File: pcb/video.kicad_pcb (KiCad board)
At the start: 4 copper layers, 159.9 x 99.9 mm, 174 parts, among them J1 09031966921, J3 Conn_01x06, J4 Conn_01x06, J5 Conn_01x06, J6 Conn_01x06, J7 DB15_Female_HighDensity, J8 HDMI_A, U1 NCP115, U10 NCA9306DPH, U2 LP3853ESX-3.3/NOPB, U3 LCMXO2-1200HC-4TG100I, U4 LCMXO2-7000HC-4TG144C, U5 THS8136, U6 TFP410PAP, U7 ESD224DQA, U8 ESD224DQA, U9 PCA9540BDP, X1 ASV-xxxMHz

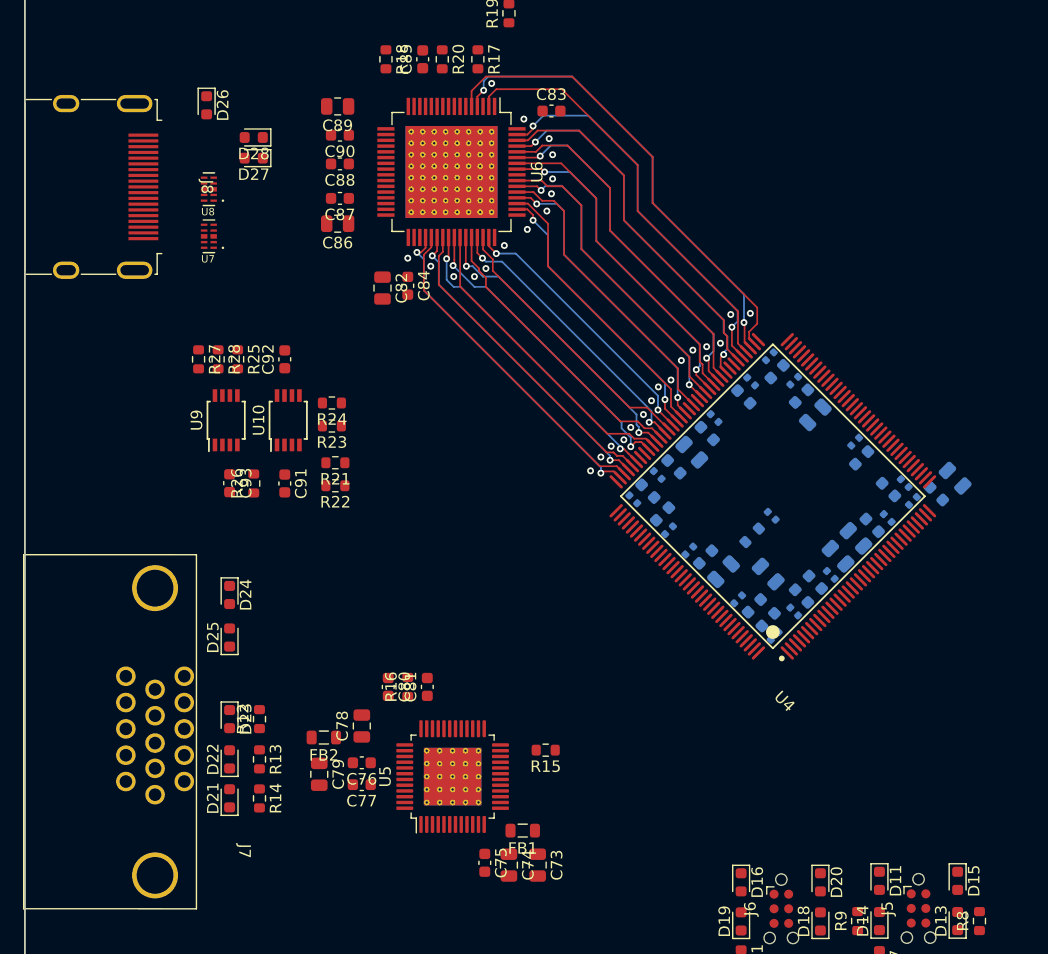
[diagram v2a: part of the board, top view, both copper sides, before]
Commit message: change the bank for the hdmi interface
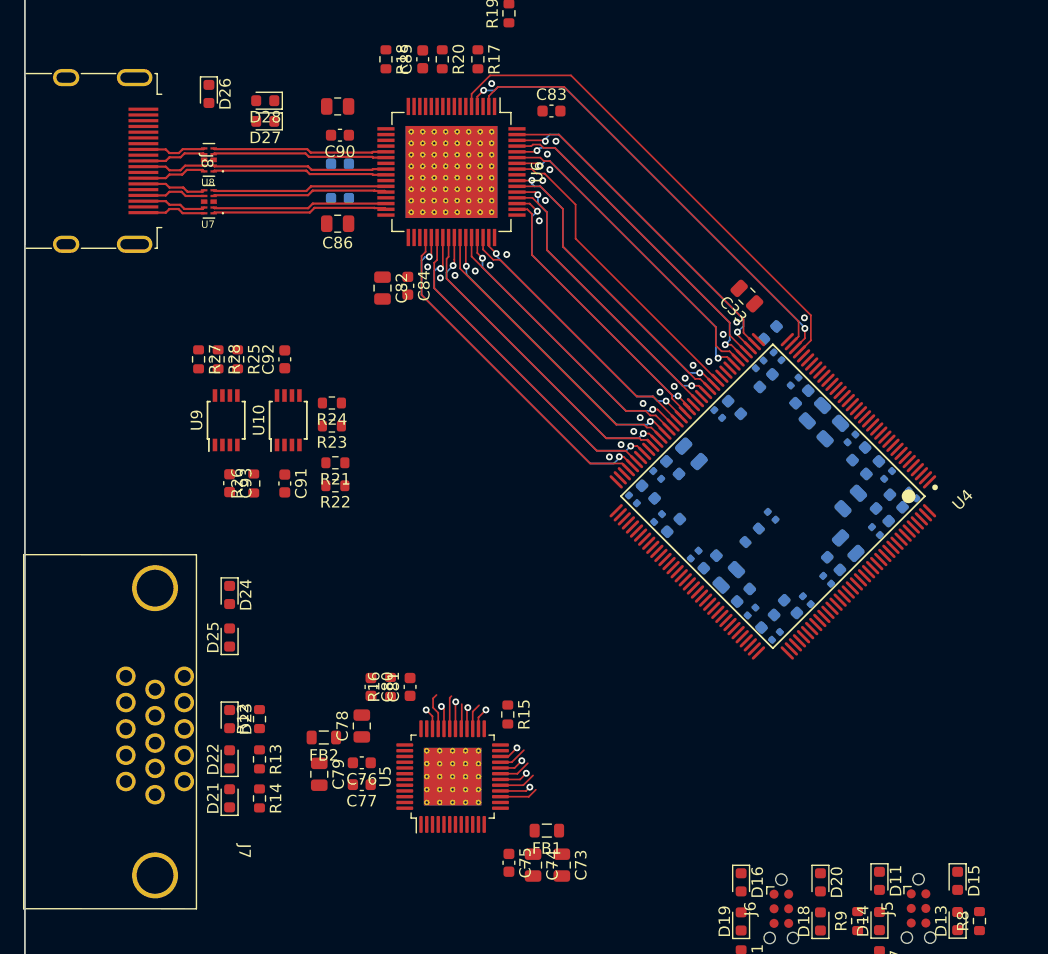
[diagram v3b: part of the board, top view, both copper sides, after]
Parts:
- C33: moved to F.Cu
- C87, C88: moved to B.Cu
- moved C33 24.1 mm to (117.9, 78.6), turned to 135 degrees
- moved C37 20.1 mm to (119.9, 81.8), turned to 45 degrees
- moved C41 17.2 mm to (120.5, 83.9), turned to -45 degrees
- moved C40 17.2 mm to (108.0, 96.3), turned to -45 degrees
- moved C39 17.2 mm to (120.4, 108.2), turned to 45 degrees
- moved C38 17.2 mm to (132.3, 95.9), turned to 135 degrees
- moved C62 16.3 mm to (119.0, 84.6), turned to -135 degrees
- moved C35 15.4 mm to (119.7, 106.9), turned to 45 degrees
- moved C34 15.3 mm to (109.3, 95.7), turned to -45 degrees
- moved C36 15.2 mm to (130.9, 96.5), turned to 135 degrees
- moved C63 14.5 mm to (110.1, 94.2), turned to -45 degrees
- moved C71 14.4 mm to (130.2, 94.2), turned to -135 degrees
- moved C49 14.4 mm to (118.3, 106.1), turned to 45 degrees
- moved C51 14.4 mm to (110.2, 97.9), turned to 45 degrees
- moved C58 14.4 mm to (122.0, 86.1), turned to -135 degrees
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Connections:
- net /HDMI frontend/D0_M renamed /HDMI frontend/D0_N
- net /HDMI frontend/D1_M renamed /HDMI frontend/D1_N
- net /HDMI frontend/D2_M renamed /HDMI frontend/D2_N
- net /HDMI frontend/DC_M renamed /HDMI frontend/DC_N
- net /HDMI frontend/TX0_M renamed /HDMI frontend/TX0_N
- net /HDMI frontend/TX1_M renamed /HDMI frontend/TX1_N
- net /HDMI frontend/TX2_M renamed /HDMI frontend/TX2_N
- net /HDMI frontend/TXC_M renamed /HDMI frontend/TXC_N
- U4 pad 100: HDMI_D18 -> VGA_B6
- U4 pad 103: HDMI_D19 -> VGA_B7
- U4 pad 104: HDMI_D20 -> unconnected-(U4B-PR3B/R_GPLLC_IN/(DQ0))
- U4 pad 105: HDMI_D21 -> unconnected-(U4B-PR3A/R_GPLLT_IN/(DQ0))
- U4 pad 106: HDMI_D22 -> unconnected-(U4B-PR2B/R_GPLLC_FB/(DQ0))
- U4 pad 107: HDMI_D23 -> unconnected-(U4B-PR2A/R_GPLLT_FB/(DQ0))
- U4 pad 33: unconnected-(U4D-PL24B) -> HDMI_VSYNC
- U4 pad 34: unconnected-(U4D-PL25A) -> HDMI_HSYNC
- U4 pad 35: unconnected-(U4D-PL25B) -> HDMI_DE
- U4 pad 38: unconnected-(U4C-PB4A) -> HDMI_D0
- U4 pad 39: unconnected-(U4C-PB4B) -> HDMI_D1
- U4 pad 40: unconnected-(U4C-PB6A/CSSPIN) -> HDMI_D2
- U4 pad 41: unconnected-(U4C-PB6B) -> HDMI_D3
- U4 pad 42: unconnected-(U4C-PB9A) -> HDMI_D4
- U4 pad 43: unconnected-(U4C-PB9B) -> HDMI_D5
- U4 pad 47: unconnected-(U4C-PB13A) -> HDMI_CLK
- U4 pad 48: unconnected-(U4C-PB13B) -> HDMI_D6
- U4 pad 49: unconnected-(U4C-PB16A/PCLKT2_0) -> HDMI_D7
- U4 pad 50: unconnected-(U4C-PB16B/PCLKC2_0) -> HDMI_D8
- U4 pad 52: unconnected-(U4C-PB18A) -> HDMI_D9
- U4 pad 54: unconnected-(U4C-PB18B) -> HDMI_D10
- U4 pad 55: unconnected-(U4C-PB23A/PCLKT2_1) -> HDMI_D11
- U4 pad 56: unconnected-(U4C-PB23B/PCLKC2_1) -> HDMI_D12
- U4 pad 57: unconnected-(U4C-PB26A) -> HDMI_D13
- U4 pad 58: unconnected-(U4C-PB26B) -> HDMI_D14
- U4 pad 59: unconnected-(U4C-PB29A) -> HDMI_D15
- U4 pad 60: unconnected-(U4C-PB29B) -> HDMI_D16
- U4 pad 61: unconnected-(U4C-PB31A) -> HDMI_D17
- U4 pad 62: unconnected-(U4C-PB31B) -> HDMI_D18
- U4 pad 63: unconnected-(U4C-PB31D) -> HDMI_D19
- U4 pad 65: unconnected-(U4C-PB35A) -> HDMI_D20
- U4 pad 67: unconnected-(U4C-PB35B) -> HDMI_D21
- U4 pad 68: unconnected-(U4C-PB37A) -> HDMI_D22
- U4 pad 69: unconnected-(U4C-PB37B) -> HDMI_D23
- U4 pad 70: unconnected-(U4C-PB38A/SN) -> /Video FPGA/SN
- U4 pad 73: unconnected-(U4B-PR24B/(DQ1)) -> VGA_G0
- U4 pad 74: HDMI_VSYNC -> VGA_G1
- U4 pad 75: HDMI_HSYNC -> VGA_G2
- U4 pad 76: HDMI_DE -> VGA_G3
- U4 pad 77: HDMI_D0 -> VGA_G4
- U4 pad 78: HDMI_D1 -> VGA_G5
- U4 pad 81: HDMI_D2 -> VGA_G6
- U4 pad 82: HDMI_D3 -> VGA_G7
- U4 pad 83: HDMI_D4 -> VGA_CLK
- U4 pad 84: HDMI_D5 -> VGA_R7
- U4 pad 85: HDMI_CLK -> VGA_R6
- U4 pad 86: HDMI_D6 -> VGA_R5
- U4 pad 87: HDMI_D7 -> VGA_R4
- U4 pad 89: HDMI_D8 -> VGA_R3
- U4 pad 91: HDMI_D9 -> VGA_R2
- U4 pad 92: HDMI_D10 -> VGA_R1
- U4 pad 93: HDMI_D11 -> VGA_R0
- U4 pad 94: HDMI_D12 -> VGA_B0
- U4 pad 95: HDMI_D13 -> VGA_B1
- U4 pad 96: HDMI_D14 -> VGA_B2
- U4 pad 97: HDMI_D15 -> VGA_B3
- U4 pad 98: HDMI_D16 -> VGA_B4
- U4 pad 99: HDMI_D17 -> VGA_B5
- U5 pad 1: VGA_B9 -> VGA_B7
- U5 pad 10: VGA_B0 -> GND
- U5 pad 13: VGA_R0 -> GND
- U5 pad 14: VGA_R1 -> GND
- U5 pad 15: VGA_R2 -> VGA_R0
- U5 pad 16: VGA_R3 -> VGA_R1
- U5 pad 17: VGA_R4 -> VGA_R2
- U5 pad 18: VGA_R5 -> VGA_R3
- U5 pad 19: VGA_R6 -> VGA_R4
- U5 pad 2: VGA_B8 -> VGA_B6
- U5 pad 20: VGA_R7 -> VGA_R5
- U5 pad 21: VGA_R8 -> VGA_R6
- U5 pad 22: VGA_R9 -> VGA_R7
- U5 pad 27: VGA_G9 -> VGA_G7
- U5 pad 28: VGA_G8 -> VGA_G6
- U5 pad 29: VGA_G7 -> VGA_G5
- U5 pad 3: VGA_B7 -> VGA_B5
- U5 pad 30: VGA_G6 -> VGA_G4
- U5 pad 31: VGA_G5 -> VGA_G3
- U5 pad 32: VGA_G4 -> VGA_G2
- U5 pad 33: VGA_G3 -> VGA_G1
- U5 pad 34: VGA_G2 -> VGA_G0
- U5 pad 35: VGA_G1 -> unconnected-(U5-G1)
- U5 pad 36: VGA_G0 -> GND
- U5 pad 4: VGA_B6 -> VGA_B4
- U5 pad 49: (no net) -> GND
- U5 pad 5: VGA_B5 -> VGA_B3
- U5 pad 6: VGA_B4 -> VGA_B2
- U5 pad 7: VGA_B3 -> VGA_B1
- U5 pad 8: VGA_B2 -> VGA_B0
- U5 pad 9: VGA_B1 -> GND
- U6 pad 65: unconnected-(U6B-EP) -> GND
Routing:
- net /HDMI frontend/TX2_P: track 0.00 -> 15.2 mm
- net /HDMI frontend/TX1_P: track 0.00 -> 15.2 mm
- net /HDMI frontend/TX2_N: track 0.00 -> 15.2 mm
- net /HDMI frontend/TX1_N: track 0.00 -> 15.2 mm
- net /HDMI frontend/TXC_P: track 0.00 -> 15.2 mm
- net /HDMI frontend/TX0_P: track 0.00 -> 15.2 mm
- net /HDMI frontend/TX0_N: track 0.00 -> 15.2 mm
- net /HDMI frontend/TXC_N: track 0.00 -> 15.2 mm
- net /HDMI frontend/D0_P: track 0.00 -> 5.63 mm
- net /HDMI frontend/D1_N: track 0.00 -> 5.62 mm
- net /HDMI frontend/D2_N: track 0.00 -> 5.62 mm
- net /HDMI frontend/DC_P: track 0.00 -> 5.58 mm
- net /HDMI frontend/DC_N: track 0.00 -> 5.58 mm
- net /HDMI frontend/D0_N: track 0.00 -> 5.58 mm
- net /HDMI frontend/D1_P: track 0.00 -> 5.56 mm
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
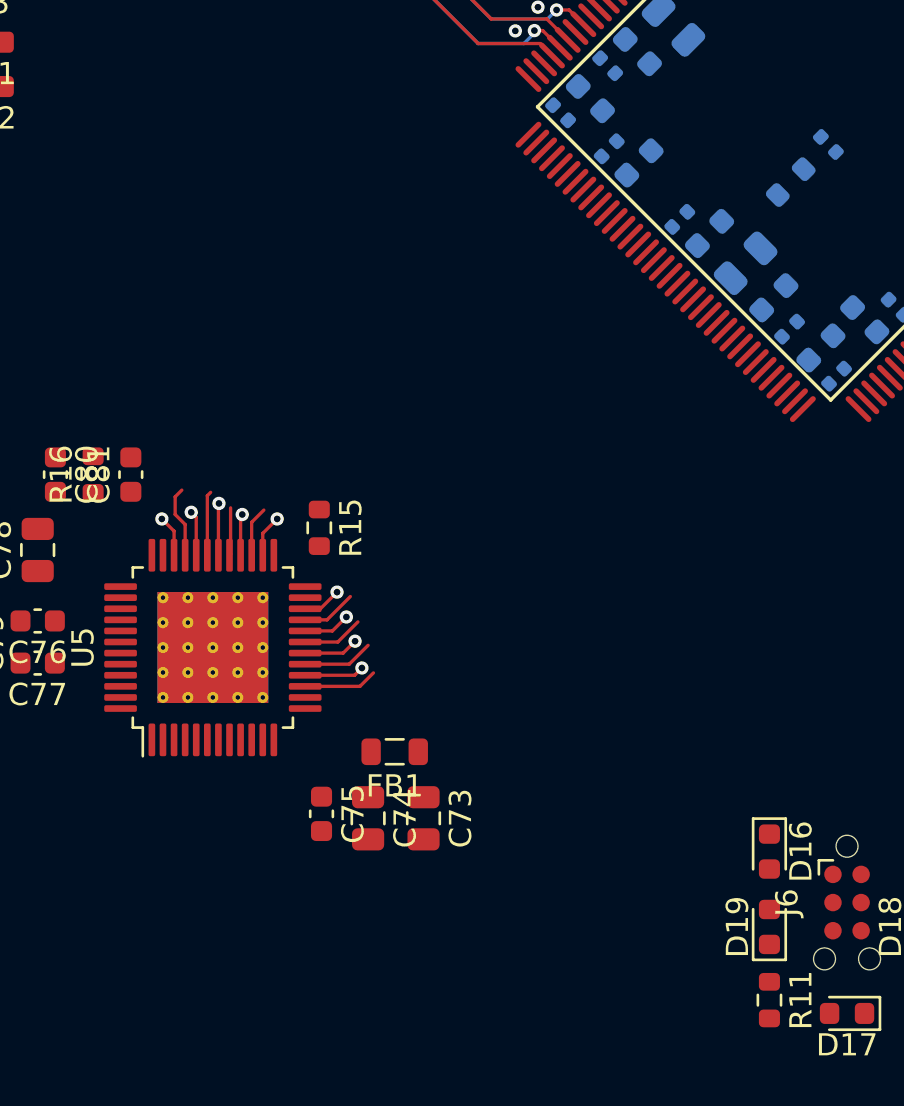
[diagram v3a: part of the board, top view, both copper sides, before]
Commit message: add traces to the vga interface minimizing crosstalk
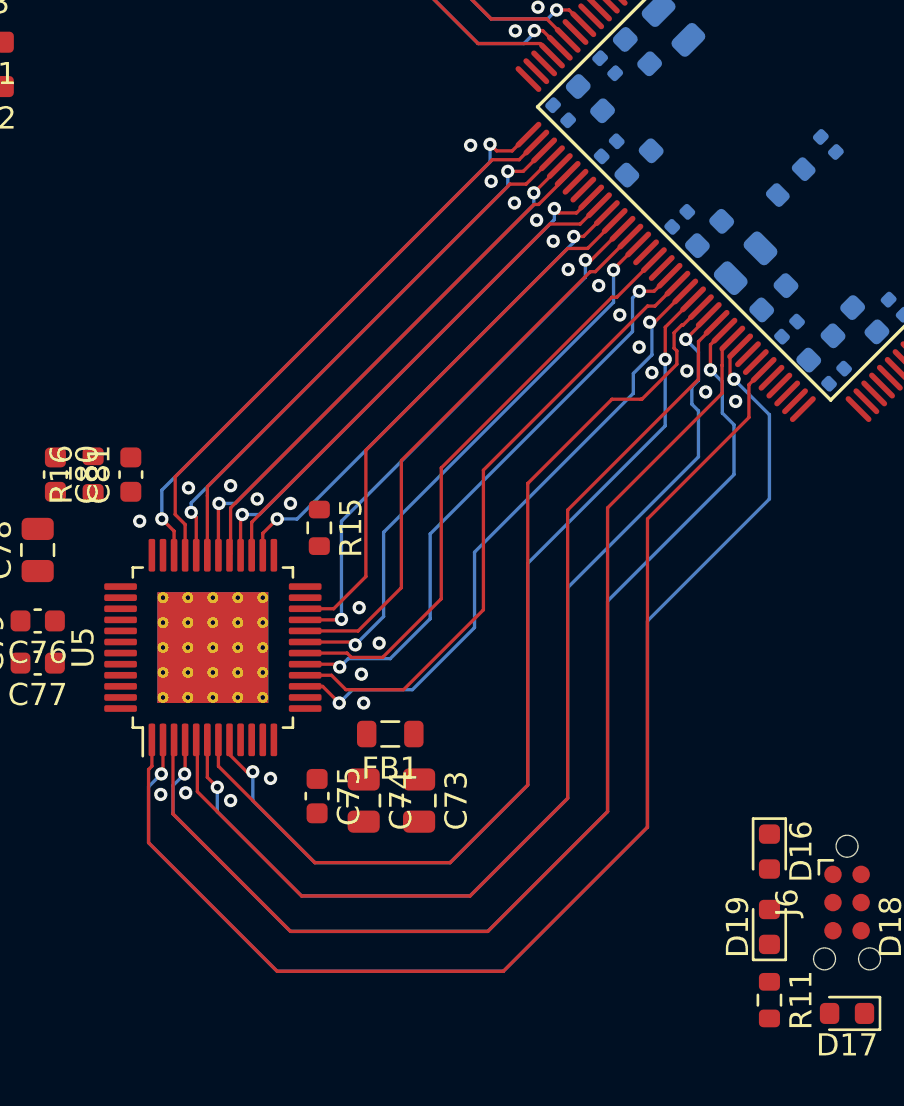
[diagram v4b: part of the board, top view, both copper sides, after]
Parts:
- moved C75 0.82 mm to (97.0, 127.1)
- moved C73 0.82 mm to (101.6, 127.3)
- moved C74 0.82 mm to (99.1, 127.3)
- moved FB1 0.82 mm to (100.3, 124.3)
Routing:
- net VGA_B6: track 0.00 -> 57.4 mm, vias 0 -> 2
- net VGA_B7: track 0.00 -> 55.1 mm
- net VGA_B4: track 0.00 -> 52.3 mm, vias 0 -> 2
- net VGA_B5: track 0.00 -> 51.1 mm
- net VGA_B2: track 0.00 -> 47.8 mm, vias 0 -> 2
- net VGA_B3: track 0.00 -> 47.1 mm
- net VGA_B1: track 0.00 -> 44.1 mm
- net VGA_B0: track 0.00 -> 43.3 mm, vias 0 -> 2
- net VGA_R1: track 2.69 -> 28.3 mm, vias 1 -> 0
- net VGA_R0: track 3.33 -> 28.7 mm, vias 0 -> 2
- net VGA_G0: track 1.87 -> 27.1 mm, vias 1 -> 2
- net VGA_R3: track 2.47 -> 26.7 mm, vias 1 -> 0
- net VGA_R2: track 3.19 -> 26.9 mm, vias 0 -> 2
- net VGA_G2: track 2.03 -> 25.4 mm, vias 1 -> 2
- net VGA_R5: track 2.12 -> 25.4 mm, vias 1 -> 0
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
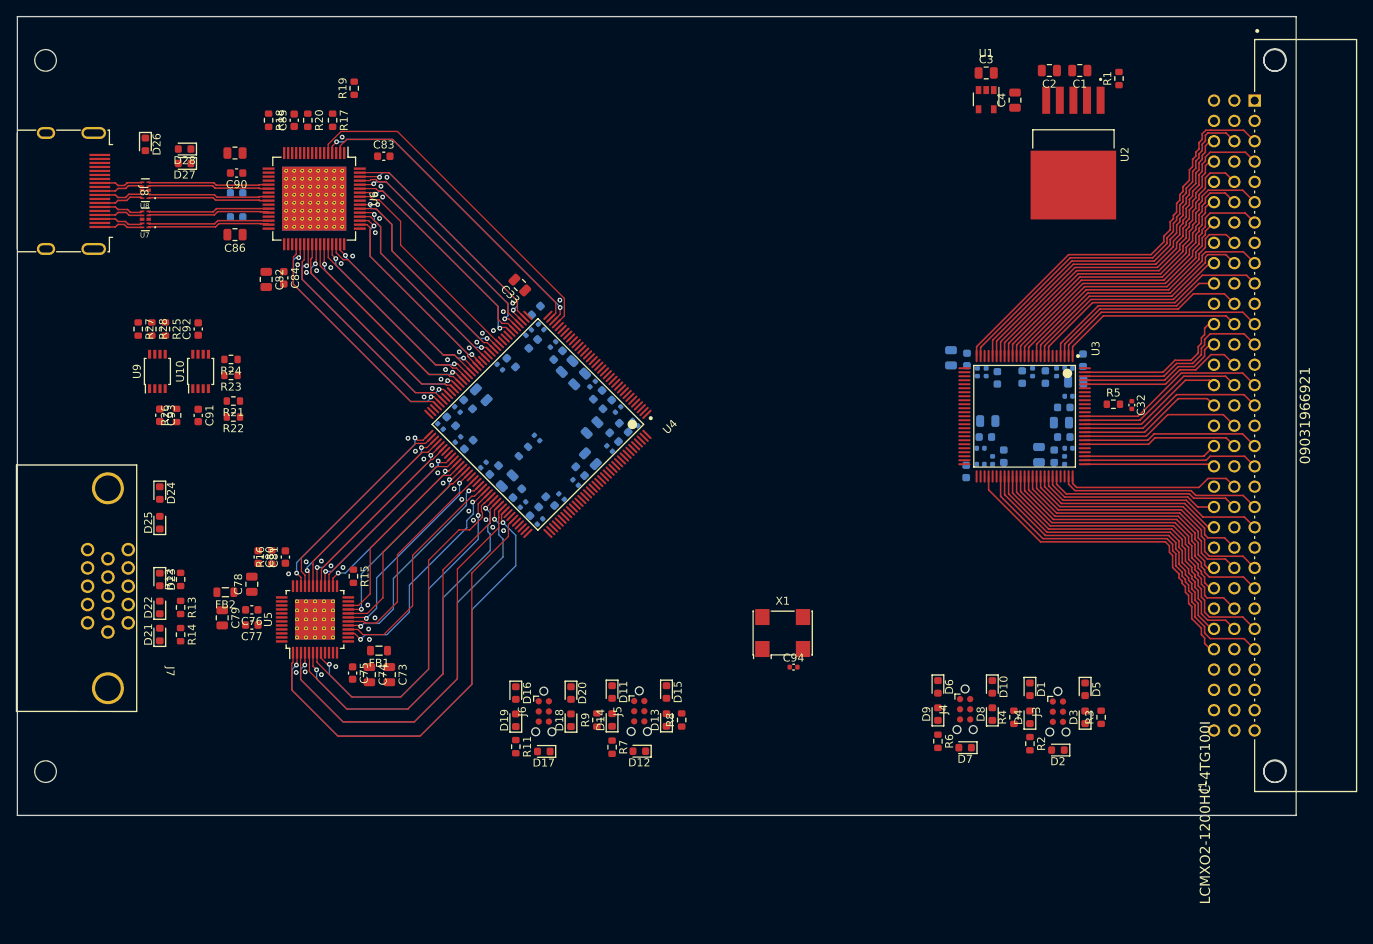
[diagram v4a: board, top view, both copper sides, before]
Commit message: add traces for the bus with crosstalk reduction
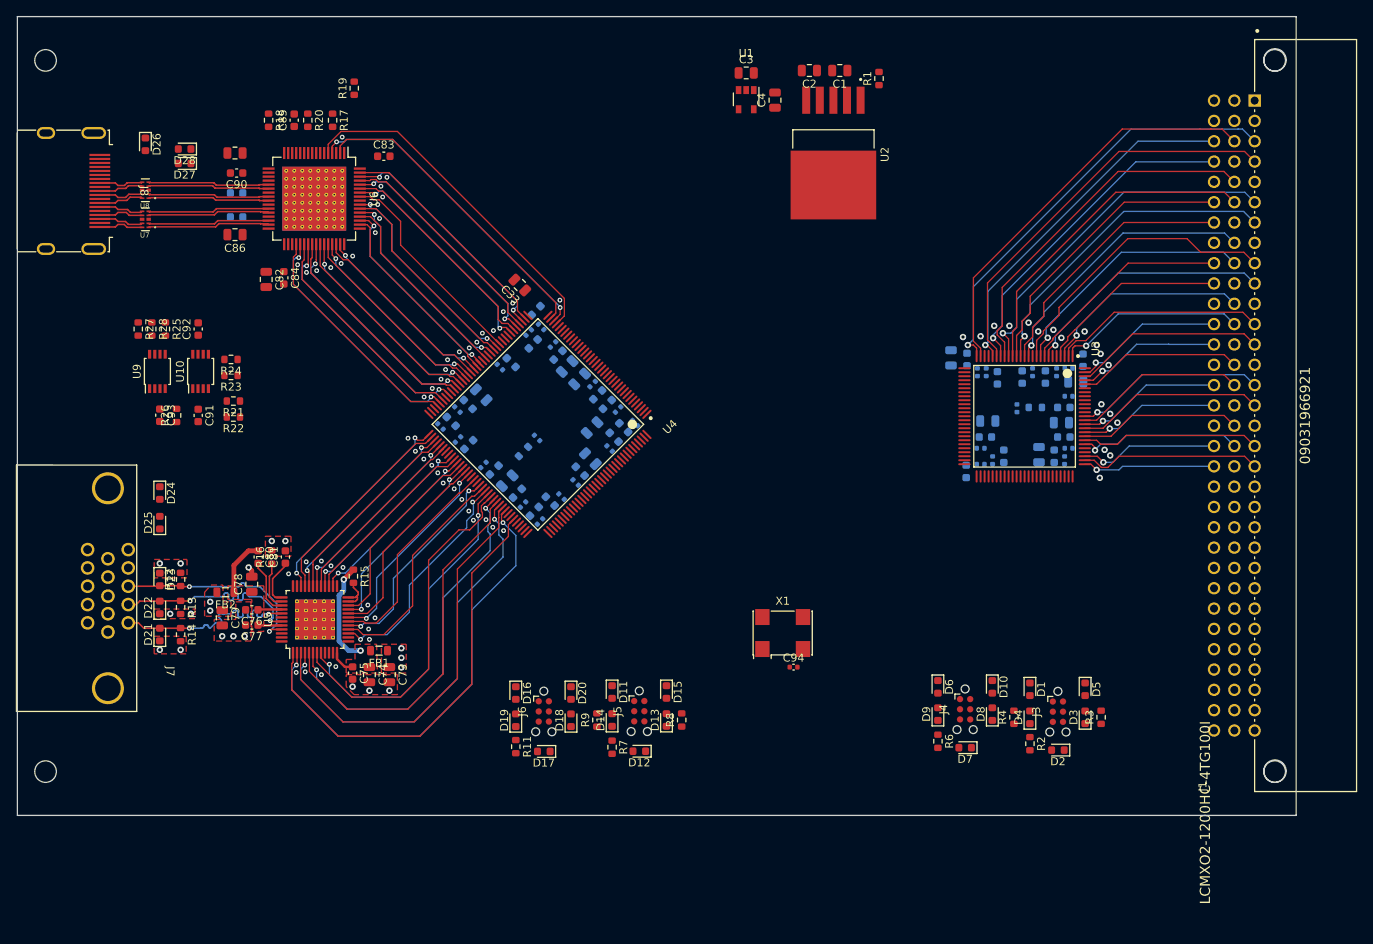
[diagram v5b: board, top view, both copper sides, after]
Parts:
- C32, R5: moved to B.Cu
- moved C1 30.0 mm to (157.9, 51.8)
- moved C2 30.0 mm to (154.1, 51.8)
- moved C3 30.0 mm to (146.2, 52.1)
- moved C4 30.0 mm to (149.8, 55.5)
- moved R1 30.0 mm to (162.8, 52.8)
- moved U1 30.0 mm to (146.2, 54.3)
- moved U2 30.0 mm to (157.1, 66.1)
- moved C32 14.4 mm to (180.0, 94.0)
- moved R5 9.77 mm to (182.3, 93.9), turned to 180 degrees
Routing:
- net CONN_51: track 46.3 -> 0.00 mm
- net CONN_48: track 43.1 -> 0.00 mm
- net CONN_52: track 42.7 -> 0.00 mm
- net CONN_49: track 41.1 -> 0.00 mm
- net CONN_50: track 39.1 -> 0.00 mm
- net CONN_47: track 38.0 -> 0.00 mm
- net CONN_45: track 37.4 -> 0.00 mm
- net CONN_42: track 34.2 -> 0.00 mm
- net CONN_46: track 33.3 -> 0.00 mm
- net CONN_43: track 32.2 -> 0.00 mm
- net CONN_44: track 30.5 -> 0.00 mm
- net CONN_41: track 29.2 -> 0.00 mm
- net CONN_39: track 29.1 -> 0.00 mm
- net /VGA frontend/RED: track 0.00 -> 25.6 mm, vias 0 -> 2
- net /VGA frontend/GREEN: track 0.00 -> 25.6 mm, vias 0 -> 2
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- added copper zone on F.Cu, net +1V8
- added copper zone on F.Cu, net +3V3
- added copper zone on F.Cu, net /VGA frontend/AVDD
- added copper zone on F.Cu, net /VGA frontend/DVDD
- added copper zone on F.Cu, net GND
